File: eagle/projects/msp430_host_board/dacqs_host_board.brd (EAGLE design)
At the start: 127 x 102 mm, 181 parts, among them J1 MOL-SL-4-RA, J10 MOL-SL-3-V, J11 MOL-SL-2-V, J13 JST-PH-2TH-RA, J14 USB_MICROB_RECPT, J16 MOL-SL-2-RA, J17 CLM-112-02-L-D-IMU-MOUNT_IMU, J18 MOLSL-7-RA, J2 MOL-SL-4-RA, J3 MOL-SL-4-RA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

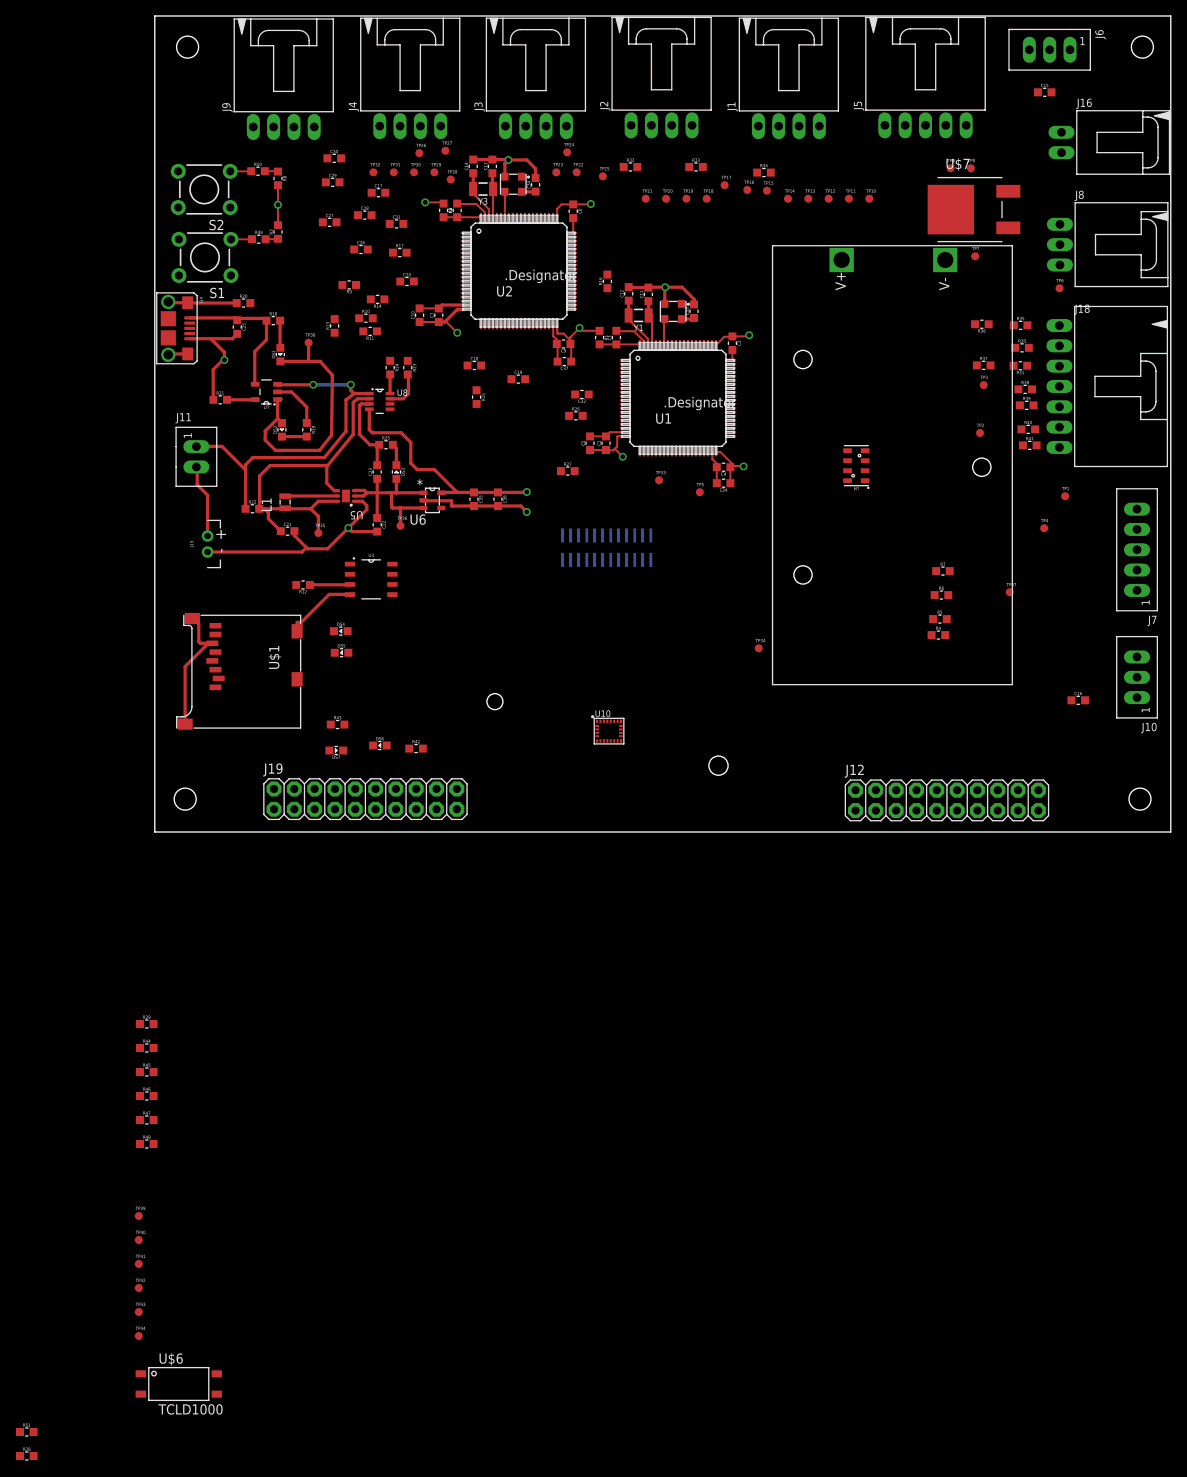
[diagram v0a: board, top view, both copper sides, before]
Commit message: Worked on cutdown routing and placement
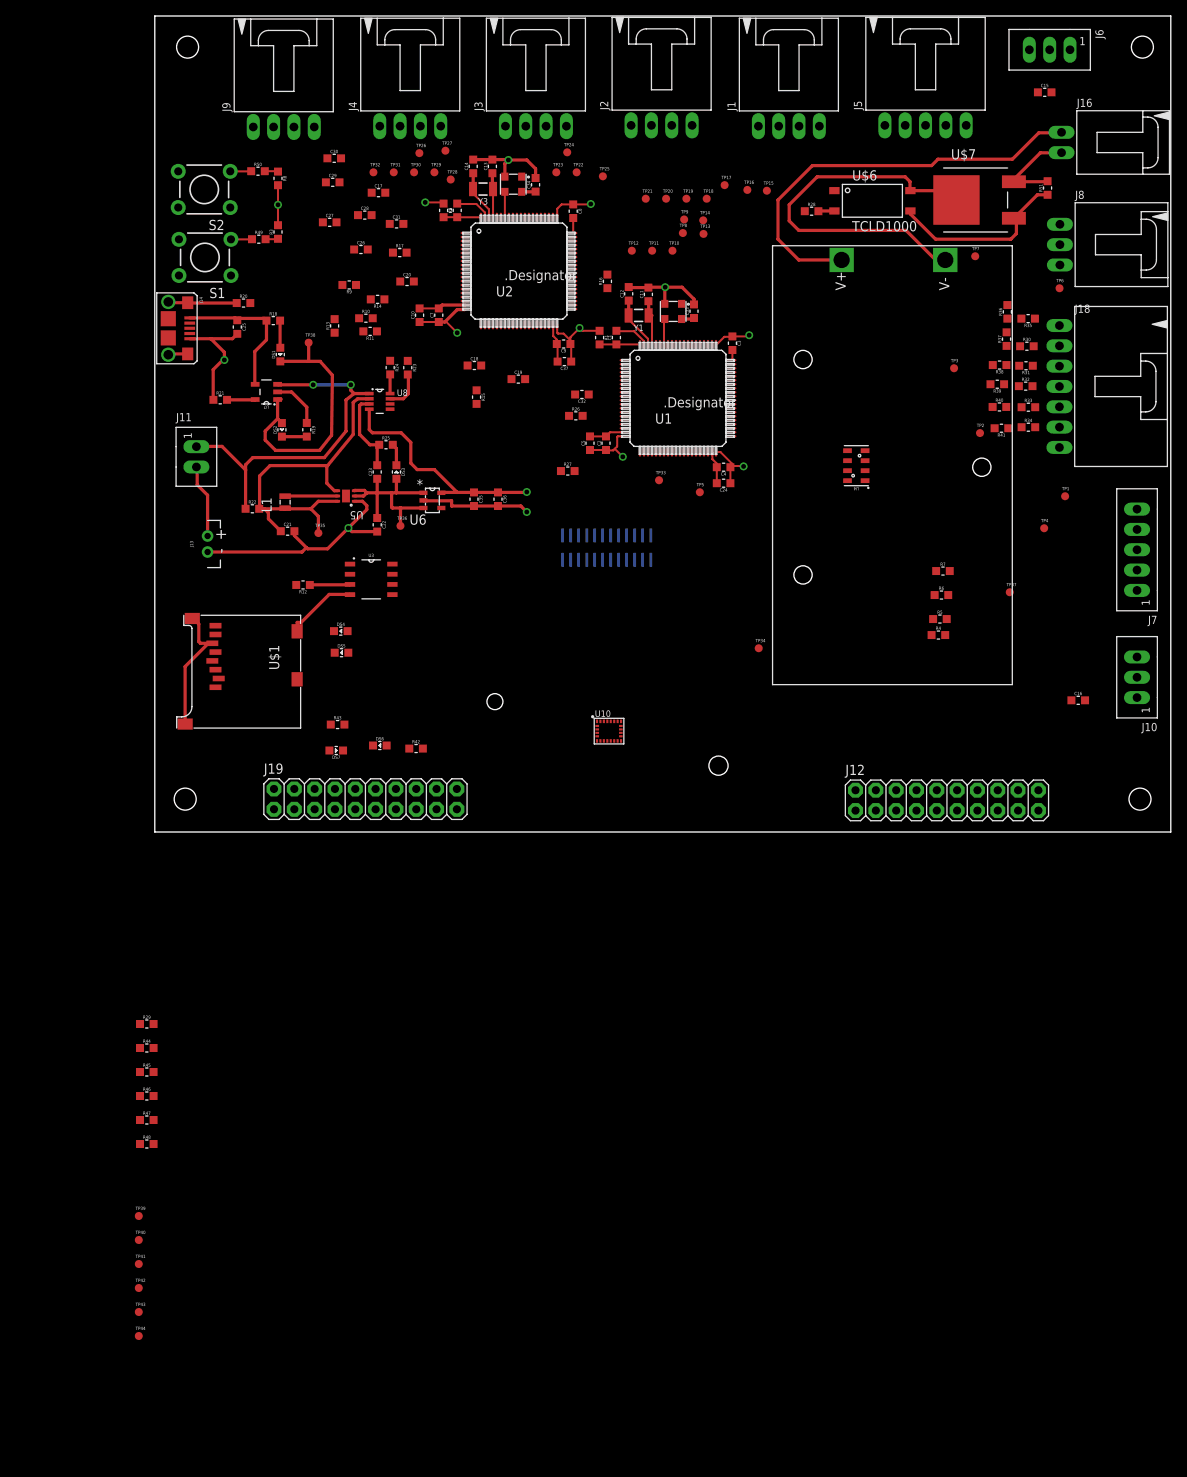
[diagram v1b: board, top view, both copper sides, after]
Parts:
- moved R51 201.2 mm to (111.6, 80.5), turned to 90 degrees
- moved R28 183.9 mm to (82.1, 77.6)
- moved U$6 171.4 mm to (89.7, 78.9)
- moved R32 56.5 mm to (108.9, 55.7)
- moved R33 51.3 mm to (109.2, 53.1)
- moved R34 45.9 mm to (109.2, 50.6)
- moved TP8 36.9 mm to (66.0, 74.9)
- moved TP9 33.9 mm to (66.2, 76.6)
- moved TP10 25.4 mm to (64.7, 72.7)
- moved TP12 25.4 mm to (59.6, 72.7)
- moved TP11 25.4 mm to (62.2, 72.7)
- moved TP13 13.8 mm to (68.6, 74.8)
- moved TP14 10.9 mm to (68.5, 76.5)
- moved R40 4.56 mm to (105.6, 53.1)
- moved R39 4.53 mm to (105.3, 56.0), turned to 180 degrees
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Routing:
- net VBAT_POS: track 0.00 -> 52.9 mm
- net 9V_GND: track 0.00 -> 46.2 mm
- net CUTDOWN_GATE: track 0.00 -> 22.7 mm
- net CUTDOWN_DRAIN: track 0.00 -> 11.9 mm
- net OPTO_OUT: track 0.00 -> 2.01 mm

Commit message: Updating placement and routing for sensors
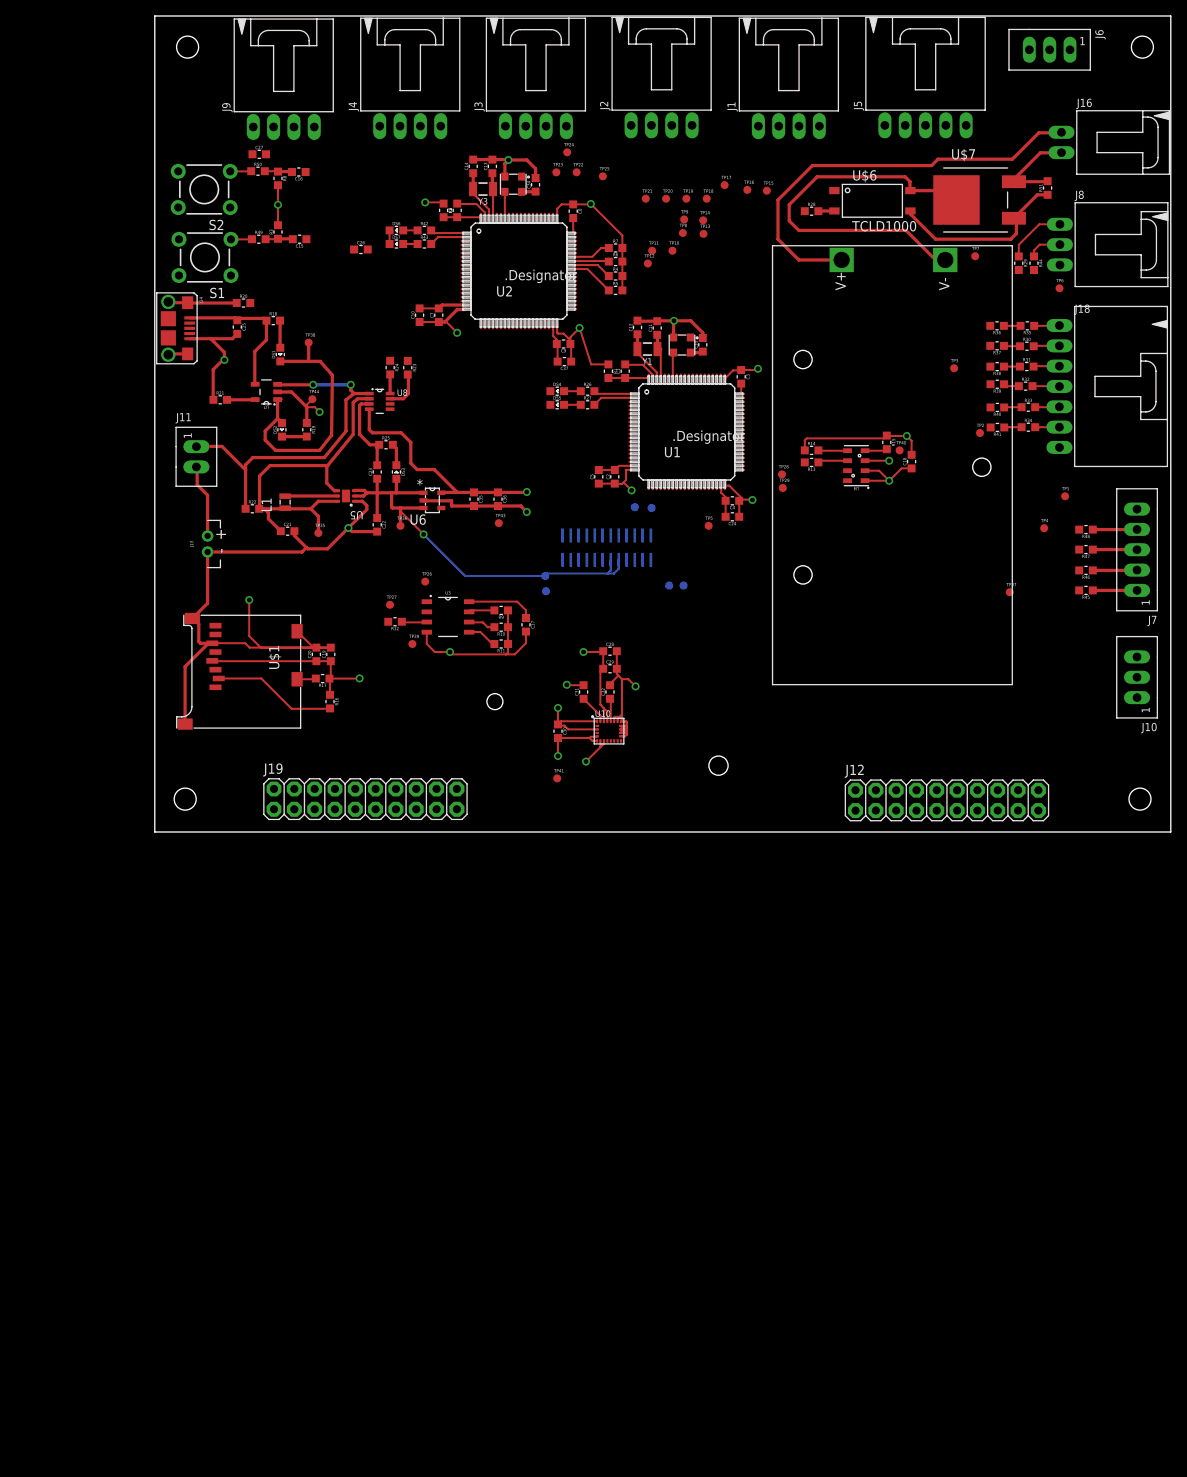
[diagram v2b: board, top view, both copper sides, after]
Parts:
- moved R44 148.1 mm to (109.9, 71.1), turned to 270 degrees
- moved R29 144.7 mm to (108.0, 71.1), turned to 270 degrees
- moved R48 140.3 mm to (116.4, 37.8), turned to 180 degrees
- moved R47 137.4 mm to (116.4, 35.3), turned to 180 degrees
- moved TP40 137.1 mm to (93.1, 47.7)
- moved R46 134.5 mm to (116.4, 32.7), turned to 180 degrees
- moved R45 131.9 mm to (116.4, 30.2), turned to 180 degrees
- moved TP44 119.1 mm to (19.7, 54.1)
- moved C16 117.7 mm to (18.0, 82.5), turned to 180 degrees
- moved TP43 108.4 mm to (43.0, 38.6)
- moved TP42 100.9 mm to (48.9, 30.1), flipped to the bottom
- moved C15 94.9 mm to (18.1, 74.1), turned to 180 degrees
- moved TP41 80.1 mm to (50.3, 6.70)
- moved TP39 79.3 mm to (32.2, 23.5)
- moved C30 76.9 mm to (50.4, 12.6), turned to 270 degrees
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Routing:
- net GND: track 156.9 -> 270.0 mm, vias 5 -> 13
- net +3V3: track 82.7 -> 170.7 mm, vias 9 -> 14
- net +5V: track 25.2 -> 59.2 mm, vias 0 -> 1
- net SD_CS: track 0.00 -> 15.5 mm
- net ACT_SPEED_IN_0: track 0.00 -> 7.65 mm
- net SENSE_SDA_1: track 0.00 -> 5.61 mm
- net COMMS_SCLK_0: track 0.00 -> 5.55 mm
- net COMMS_MOSI_0: track 0.00 -> 5.54 mm
- net COMMS_MISO_0: track 0.00 -> 5.54 mm
- net COMMS_SS_0: track 0.00 -> 5.53 mm
- net LED_BLUE_RES_1: track 0.00 -> 5.19 mm
- net SENSE_SCL_1: track 0.00 -> 5.07 mm
- net SENSE_SCL_2: track 0.00 -> 4.97 mm
- net LED_GREEN_RES_1: track 0.00 -> 4.96 mm
- net LED_BLUE_RES_2: track 0.00 -> 4.61 mm
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
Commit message: Modified IMU2 interrupt pinout
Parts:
- moved J19 2.70 mm to (23.6, 4.20), flipped to the bottom
- moved J12 2.62 mm to (96.6, 5.00), flipped to the bottom
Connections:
- net IMU2_DEN: now also J12.19; no longer J12.11
- net IMU2_DRDY: now also J12.11; no longer J12.13
- net IMU2_INT1: now also J12.15; no longer J12.7
- net IMU2_INT2: now also J12.17; no longer J12.9
- net IMU2_INT_M: now also J12.13; no longer J12.15
- net P7.0: now also J12.7; no longer J12.17
- net P7.1: now also J12.9; no longer J12.19
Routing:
- net IMU2_DRDY: track 0.00 -> 49.3 mm
- net IMU2_INT_M: track 0.00 -> 45.3 mm
- net IMU2_INT1: track 0.00 -> 41.6 mm
- net IMU2_INT2: track 0.00 -> 37.9 mm
- net IMU2_DEN: track 0.00 -> 34.2 mm

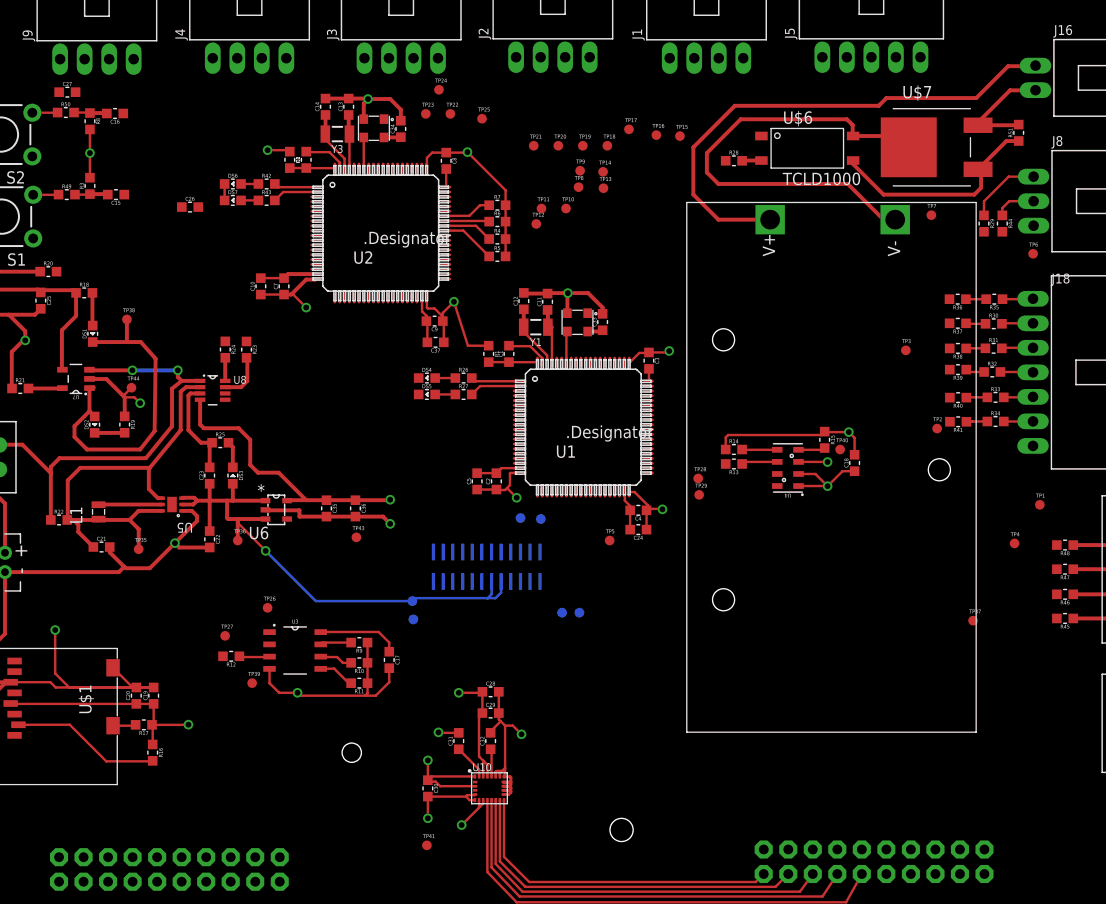
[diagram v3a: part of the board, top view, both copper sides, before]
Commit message: placing testpoints
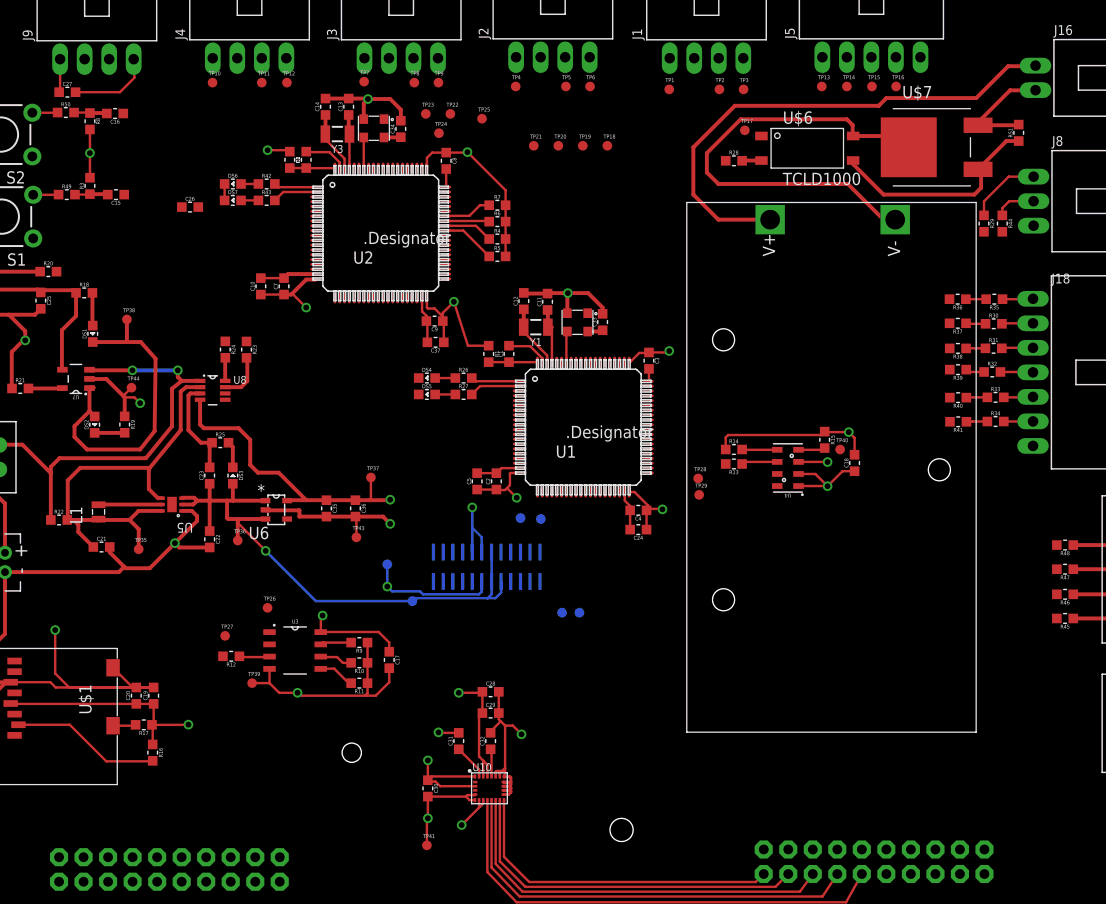
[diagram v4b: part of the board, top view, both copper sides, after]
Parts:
- moved TP4 70.1 mm to (59.5, 85.3)
- moved TP37 64.1 mm to (44.5, 44.8)
- moved TP7 60.4 mm to (43.8, 85.8)
- moved TP1 57.7 mm to (75.4, 85.0)
- moved TP6 49.1 mm to (67.2, 85.3)
- moved TP5 47.2 mm to (64.7, 85.3)
- moved TP2 41.7 mm to (80.6, 85.0)
- moved TP10 38.9 mm to (28.1, 85.7)
- moved TP3 31.8 mm to (83.1, 85.0)
- moved TP11 31.8 mm to (33.2, 85.7)
- moved TP12 29.7 mm to (35.8, 85.7)
- moved TP14 26.8 mm to (93.8, 85.3)
- moved TP16 25.3 mm to (98.9, 85.3)
- moved TP13 24.9 mm to (91.2, 85.3)
- moved TP15 20.5 mm to (96.4, 85.3)
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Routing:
- net GND: track 270.0 -> 306.6 mm, vias 13 -> 15
- net +3V3: track 170.7 -> 178.3 mm, vias 14 -> 15
- net +5V: track 59.2 -> 62.3 mm
